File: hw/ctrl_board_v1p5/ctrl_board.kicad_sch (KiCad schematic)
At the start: 29 parts, among them J1 RaSCSI Connector, J2 OLED Connector, J3 Conn_01x06_Odd_Even, P1 Conn_02x20_Odd_Even, SW1 SW_SPST, SW2 SW_SPST, SW4 Rotary_Encoder_Switch, U1 PCA9554APW,118

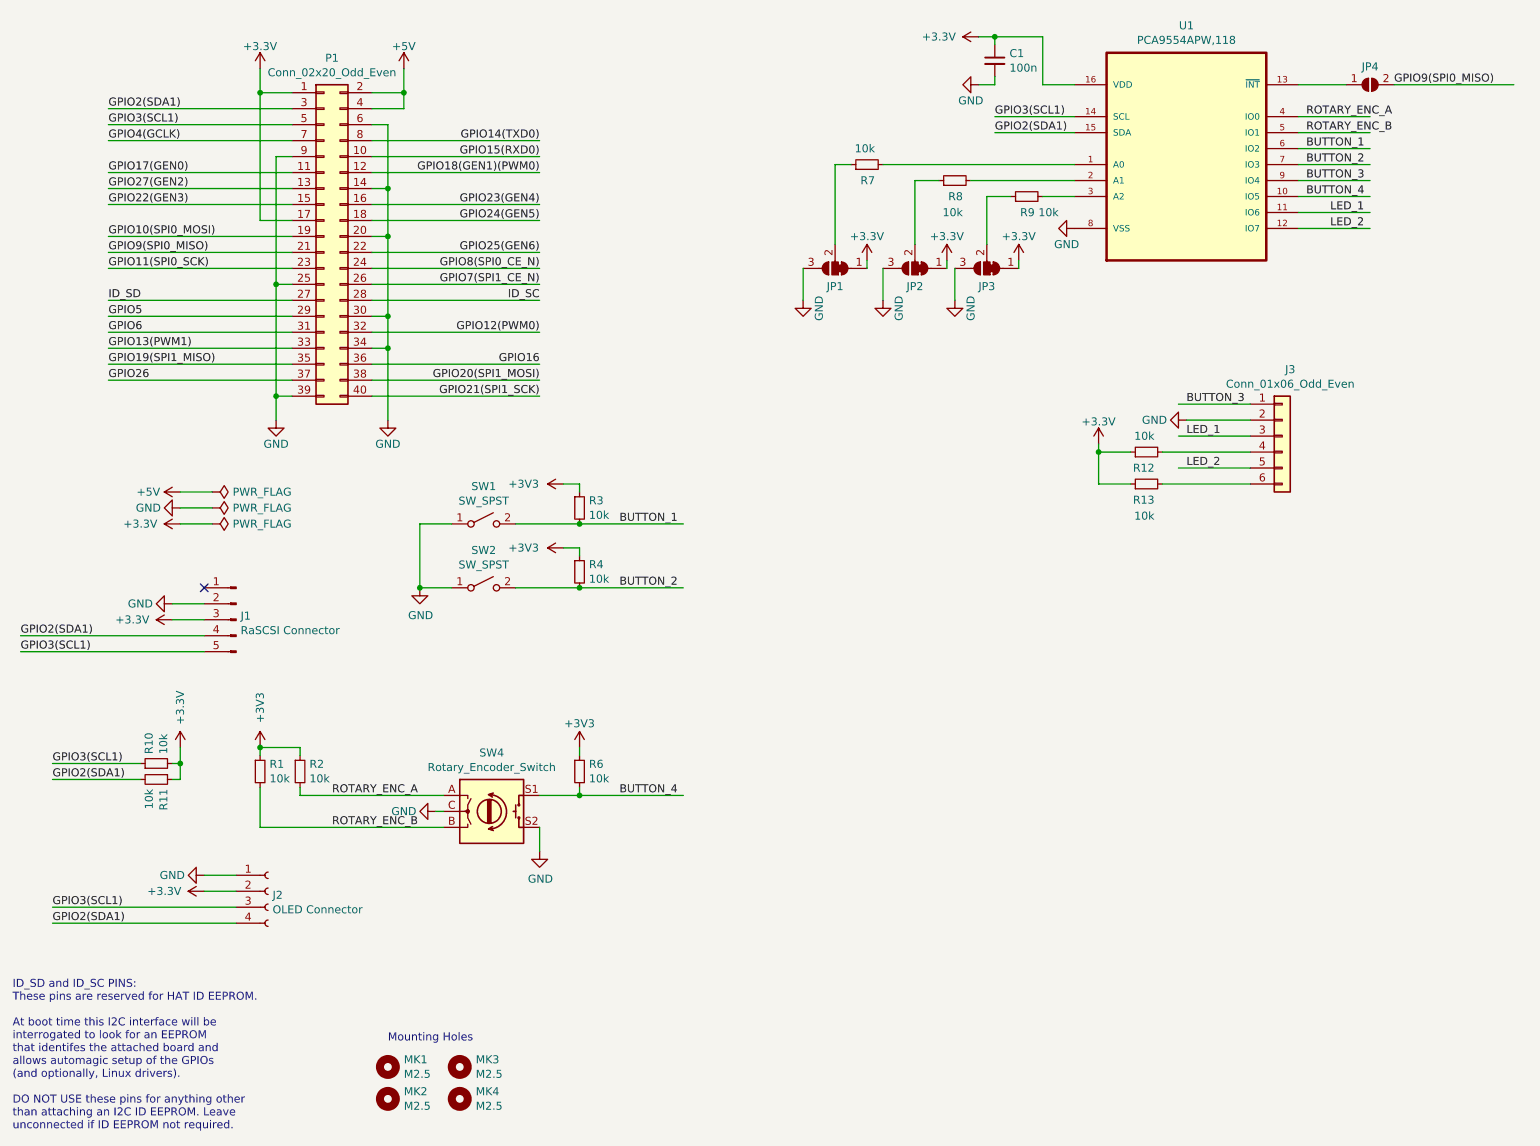
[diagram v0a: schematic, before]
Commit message: Fixed order of RaSCSI connector pinout & cleanup
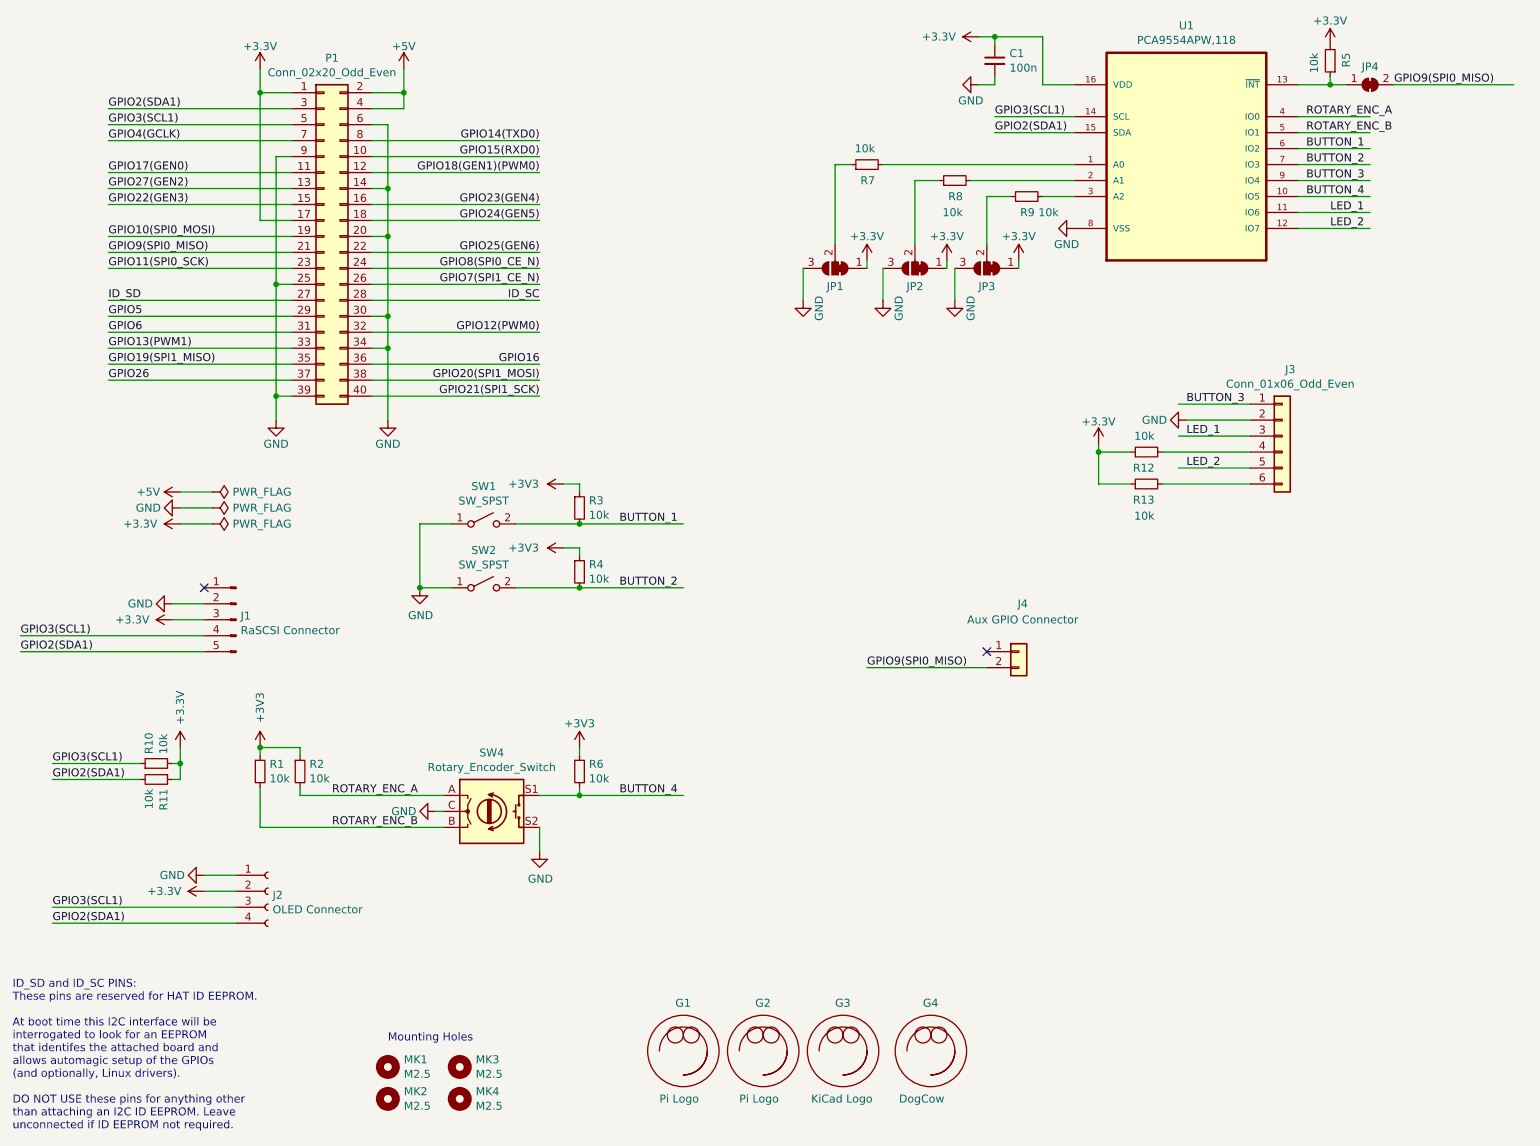
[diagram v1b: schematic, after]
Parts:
- added G1, G2: Pi Logo, mousebites:pi_logo, symbol graphics:Generic_Graphic
- added G3: KiCad Logo, Symbol:KiCad-Logo2_5mm_SilkScreen, symbol graphics:Generic_Graphic
- added G4: DogCow, mousebites:dogcow, symbol graphics:Generic_Graphic
- added J4: Aux GPIO Connector, Connector_PinHeader_2.54mm:PinHeader_1x02_P2.54mm_Vertical, symbol Connector_Generic:Conn_01x02
- added R5: 10k, Resistor_SMD:R_0805_2012Metric, symbol Device:R_Small
- JP4: footprint Jumper:SolderJumper-2_P1.3mm_Open_RoundedPad1.0x1.5mm -> Jumper:SolderJumper-2_P1.3mm_Bridged_RoundedPad1.0x1.5mm; symbol Jumper:SolderJumper_2_Open -> Jumper:SolderJumper_2_Bridged
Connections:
- net +3V3: now also R5.2
- net GPIO2(SDA1): now also J1.5 (Pin_5); no longer J1.4 (Pin_4)
- net GPIO3(SCL1): now also J1.4 (Pin_4); no longer J1.5 (Pin_5)
- net GPIO9(SPI0_MISO): now also J4.2 (Pin_2)
- net at JP4.1 (A), U1.13 (~{INT}): now also R5.1
- no-connect marks 1 -> 2
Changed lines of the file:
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@@
   (junction (at 106.68 139.7) (diameter 0) (color 0 0 0 0)
   )
+  (junction (at 226.06 26.67) (diameter 0) (color 0 0 0 0)
+  )
   (junction (at 76.2 43.18) (diameter 0) (color 0 0 0 0)
   )
+  (no_connect (at 171.45 116.84))
   (no_connect (at 46.99 106.68))
   (wire (pts (xy 22.86 157.48) (xy 52.07 157.48))
@@
     (stroke (width 0) (type default) (color 0 0 0 0))
   )
+  (wire (pts (xy 152.4 119.38) (xy 171.45 119.38))
+    (stroke (width 0) (type default) (color 0 0 0 0))
+  )
   (wire (pts (xy 147.32 39.37) (xy 149.86 39.37))
     (stroke (width 0) (type default) (color 0 0 0 0))
@@
     (stroke (width 0) (type default) (color 0 0 0 0))
   )
-  (wire (pts (xy 46.99 114.3) (xy 17.78 114.3))
+  (wire (pts (xy 46.99 116.84) (xy 17.78 116.84))
     (stroke (width 0) (type default) (color 0 0 0 0))
   )
@@
     (stroke (width 0) (type default) (color 0 0 0 0))
   )
+  (wire (pts (xy 226.06 26.67) (xy 228.6 26.67))
+    (stroke (width 0) (type default) (color 0 0 0 0))
+  )
   (wire (pts (xy 154.94 60.96) (xy 154.94 55.88))
     (stroke (width 0) (type default) (color 0 0 0 0))
@@
     (stroke (width 0) (type default) (color 0 0 0 0))
   )
-  (wire (pts (xy 220.98 26.67) (xy 228.6 26.67))
+  (wire (pts (xy 220.98 26.67) (xy 226.06 26.67))
     (stroke (width 0) (type default) (color 0 0 0 0))
   )
@@
     (stroke (width 0) (type default) (color 0 0 0 0))
   )
+  (wire (pts (xy 226.06 25.4) (xy 226.06 26.67))
+    (stroke (width 0) (type default) (color 0 0 0 0))
+  )
   (wire (pts (xy 106.68 100.33) (xy 106.68 101.6))
     (stroke (width 0) (type default) (color 0 0 0 0))
@@
     (stroke (width 0) (type default) (color 0 0 0 0))
   )
-  (wire (pts (xy 17.78 116.84) (xy 46.99 116.84))
+  (wire (pts (xy 17.78 114.3) (xy 46.99 114.3))
     (stroke (width 0) (type default) (color 0 0 0 0))
   )
@@
     (effects (font (size 1.27 1.27)) (justify right bottom))
   )
+  (label "GPIO9(SPI0_MISO)" (at 152.4 119.38 0)
+    (effects (font (size 1.27 1.27)) (justify left bottom))
+  )
   (label "GPIO4(GCLK)" (at 31.75 35.56 0)
     (effects (font (size 1.27 1.27)) (justify left bottom))
@@
     (effects (font (size 1.27 1.27)) (justify left bottom))
   )
-  (label "GPIO3(SCL1)" (at 17.78 116.84 0)
-    (effects (font (size 1.27 1.27)) (justify left bottom))
-  )
-  (label "GPIO2(SDA1)" (at 17.78 114.3 0)
+  (label "GPIO3(SCL1)" (at 17.78 114.3 0)
+    (effects (font (size 1.27 1.27)) (justify left bottom))
+  )
+  (label "GPIO2(SDA1)" (at 17.78 116.84 0)
     (effects (font (size 1.27 1.27)) (justify left bottom))
   )
@@
     (pin "1")
   )
-  (symbol (lib_id "Jumper:SolderJumper_2_Open") (at 232.41 26.67 0) (unit 1)
+  (symbol (lib_id "Jumper:SolderJumper_2_Bridged") (at 232.41 26.67 0) (unit 1)
     (in_bom yes) (on_board yes)
     (property "Reference" "JP4" (id 0) (at 232.41 23.7998 0))
@@
       (effects (font (size 1.27 1.27)) hide)
     )
-    (property "Footprint" "Jumper:SolderJumper-2_P1.3mm_Open_RoundedPad1.0x1.5mm" (id 2) (at 232.41 26.67 0)
+    (property "Footprint" "Jumper:SolderJumper-2_P1.3mm_Bridged_RoundedPad1.0x1.5mm" (id 2) (at 232.41 26.67 0)
       (effects (font (size 1.27 1.27)) hide)
     )
@@
     (pin "1")
   )
+  (symbol (lib_id "graphics:Generic_Graphic") (at 162.56 180.34 0) (unit 1)
+    (in_bom no) (on_board yes)
+    (property "Reference" "G4" (id 0) (at 161.29 172.72 0)
+      (effects (font (size 1.27 1.27)) (justify left))
+    )
+    (property "Value" "DogCow" (id 1) (at 157.48 187.96 0)
+      (effects (font (size 1.27 1.27)) (justify left))
+    )
+    (property "Footprint" "mousebites:dogcow" (id 2) (at 162.56 180.34 0)
+      (effects (font (size 1.27 1.27)) hide)
+    )
+    (property "Datasheet" "" (id 3) (at 162.56 180.34 0)
+      (effects (font (size 1.27 1.27)) hide)
+    )
+  )
+  (symbol (lib_id "graphics:Generic_Graphic") (at 148.59 180.34 0) (unit 1)
+    (in_bom no) (on_board yes)
+    (property "Reference" "G3" (id 0) (at 147.32 172.72 0)
+      (effects (font (size 1.27 1.27)) (justify left))
+    )
+    (property "Value" "KiCad Logo" (id 1) (at 143.51 187.96 0)
+      (effects (font (size 1.27 1.27)) (justify left))
+    )
+    (property "Footprint" "Symbol:KiCad-Logo2_5mm_SilkScreen" (id 2) (at 148.59 180.34 0)
+      (effects (font (size 1.27 1.27)) hide)
+    )
+    (property "Datasheet" "" (id 3) (at 148.59 180.34 0)
+      (effects (font (size 1.27 1.27)) hide)
+    )
+  )
+  (symbol (lib_id "Device:R_Small") (at 226.06 22.86 180) (unit 1)
+    (in_bom yes) (on_board yes)
+    (property "Reference" "R5" (id 0) (at 228.6 21.59 90)
+      (effects (font (size 1.27 1.27)) (justify left))
+    )
+    (property "Value" "10k" (id 1) (at 223.52 21.59 90)
+      (effects (font (size 1.27 1.27)) (justify left))
+    )
+    (property "Footprint" "Resistor_SMD:R_0805_2012Metric" (id 2) (at 226.06 22.86 0)
+      (effects (font (size 1.27 1.27)) hide)
+    )
+    (property "Datasheet" "~" (id 3) (at 226.06 22.86 0)
+      (effects (font (size 1.27 1.27)) hide)
+    )
+    (property "LCSC" "C17414" (id 4) (at 226.06 22.86 0)
+      (effects (font (size 1.27 1.27)) hide)
+    )
+    (pin "1")
+    (pin "2")
+  )
+  (symbol (lib_id "graphics:Generic_Graphic") (at 135.89 180.34 0) (unit 1)
+    (in_bom no) (on_board yes)
+    (property "Reference" "G2" (id 0) (at 134.62 172.72 0)
+      (effects (font (size 1.27 1.27)) (justify left))
+    )
+    (property "Value" "Pi Logo" (id 1) (at 132.08 187.96 0)
+      (effects (font (size 1.27 1.27)) (justify left))
+    )
+    (property "Footprint" "mousebites:pi_logo" (id 2) (at 135.89 180.34 0)
+      (effects (font (size 1.27 1.27)) hide)
+    )
+    (property "Datasheet" "" (id 3) (at 135.89 180.34 0)
+      (effects (font (size 1.27 1.27)) hide)
+    )
+  )
+  (symbol (lib_id "power:+3.3V") (at 226.06 20.32 0) (unit 1)
+    (in_bom yes) (on_board yes)
+    (property "Reference" "#PWR017" (id 0) (at 226.06 24.13 0)
+      (effects (font (size 1.27 1.27)) hide)
+    )
+    (property "Value" "+3.3V" (id 1) (at 226.06 16.51 0))
+    (property "Footprint" "" (id 2) (at 226.06 20.32 0))
+    (property "Datasheet" "" (id 3) (at 226.06 20.32 0))
+    (pin "1")
+  )
+  (symbol (lib_id "graphics:Generic_Graphic") (at 123.19 180.34 0) (unit 1)
+    (in_bom no) (on_board yes)
+    (property "Reference" "G1" (id 0) (at 121.92 172.72 0)
+      (effects (font (size 1.27 1.27)) (justify left))
+    )
+    (property "Value" "Pi Logo" (id 1) (at 119.38 187.96 0)
+      (effects (font (size 1.27 1.27)) (justify left))
+    )
+    (property "Footprint" "mousebites:pi_logo" (id 2) (at 123.19 180.34 0)
+      (effects (font (size 1.27 1.27)) hide)
+    )
+    (property "Datasheet" "" (id 3) (at 123.19 180.34 0)
+      (effects (font (size 1.27 1.27)) hide)
+    )
+  )
+  (symbol (lib_id "Connector_Generic:Conn_01x02") (at 176.53 116.84 0) (unit 1)
+    (in_bom yes) (on_board yes) (fields_autoplaced)
+    (property "Reference" "J4" (id 0) (at 177.165 109.22 0))
+    (property "Value" "Aux GPIO Connector" (id 1) (at 177.165 111.76 0))
+    (property "Footprint" "Connector_PinHeader_2.54mm:PinHeader_1x02_P2.54mm_Vertical" (id 2) (at 176.53 116.84 0)
+      (effects (font (size 1.27 1.27)) hide)
+    )
+    (property "Datasheet" "~" (id 3) (at 176.53 116.84 0)
+      (effects (font (size 1.27 1.27)) hide)
+    )
+    (pin "1")
+    (pin "2")
+  )
   (sheet_instances
     (path "/" (page "1"))
@@
       (reference "#PWR016") (unit 1) (value "+3V3") (footprint "")
     )
+    (path "/c21404c2-c0a8-47c1-b84b-d5bbab3079a4"
+      (reference "#PWR017") (unit 1) (value "+3.3V") (footprint "")
+    )
     (path "/00000000-0000-0000-0000-000061bb0926"
       (reference "#PWR018") (unit 1) (value "+3V3") (footprint "")
@@
       (reference "C1") (unit 1) (value "100n") (footprint "Capacitor_SMD:C_0805_2012Metric")
     )
+    (path "/cd0adfb4-aa4a-4c8a-9c2e-f167e56d3aa5"
+      (reference "G1") (unit 1) (value "Pi Logo") (footprint "mousebites:pi_logo")
+    )
+    (path "/b9484956-77a4-43e4-81d4-681afb826cb0"
+      (reference "G2") (unit 1) (value "Pi Logo") (footprint "mousebites:pi_logo")
+    )
+    (path "/6158f367-f08b-40da-8469-9ab484dcabf4"
+      (reference "G3") (unit 1) (value "KiCad Logo") (footprint "Symbol:KiCad-Logo2_5mm_SilkScreen")
+    )
+    (path "/2a4d7fc8-8ff6-4314-a7da-5481b9c81e99"
+      (reference "G4") (unit 1) (value "DogCow") (footprint "mousebites:dogcow")
+    )
     (path "/00000000-0000-0000-0000-000061b5acde"
       (reference "J1") (unit 1) (value "RaSCSI Connector") (footprint "Connector_PinHeader_2.54mm:PinHeader_1x05_P2.54mm_Vertical")
@@
       (reference "J3") (unit 1) (value "Conn_01x06_Odd_Even") (footprint "Connector_PinHeader_2.54mm:PinHeader_1x06_P2.54mm_Vertical")
     )
+    (path "/e1110524-9d88-4fa9-afec-1859834e2f21"
+      (reference "J4") (unit 1) (value "Aux GPIO Connector") (footprint "Connector_PinHeader_2.54mm:PinHeader_1x02_P2.54mm_Vertical")
+    )
     (path "/00000000-0000-0000-0000-000061d138dd"
       (reference "JP1") (unit 1) (value "SolderJumper_3_Bridged12") (footprint "Jumper:SolderJumper-3_P1.3mm_Bridged12_RoundedPad1.0x1.5mm")
@@
     )
     (path "/00000000-0000-0000-0000-000061cf258a"
-      (reference "JP4") (unit 1) (value "SolderJumper_2_Open") (footprint "Jumper:SolderJumper-2_P1.3mm_Open_RoundedPad1.0x1.5mm")
+      (reference "JP4") (unit 1) (value "SolderJumper_2_Open") (footprint "Jumper:SolderJumper-2_P1.3mm_Bridged_RoundedPad1.0x1.5mm")
     )
     (path "/00000000-0000-0000-0000-00005834fb2e"
@@
       (reference "R4") (unit 1) (value "10k") (footprint "Resistor_SMD:R_0805_2012Metric")
     )
+    (path "/8dd785d1-511d-4538-964b-312a69d957a7"
+      (reference "R5") (unit 1) (value "10k") (footprint "Resistor_SMD:R_0805_2012Metric")
+    )
     (path "/00000000-0000-0000-0000-000061bb0920"
